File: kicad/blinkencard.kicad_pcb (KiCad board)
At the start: 2 copper layers, 88.9 x 50.8 mm, 94 parts, among them J1 USB_B_Micro, J2 Conn_02x04_Odd_Even, Q1 BC847, Q2 BC847, Q3 BC847, Q4 BC847, Q5 BC847, SW1 0, SW2 1, SW3 LEFT, SW4 RIGHT, U1 ICE40UP5K-SG48ITR, U2 ESP32-WROOM-32, U3 AP7361C-33E, U4 MIC5504-1.2YM5

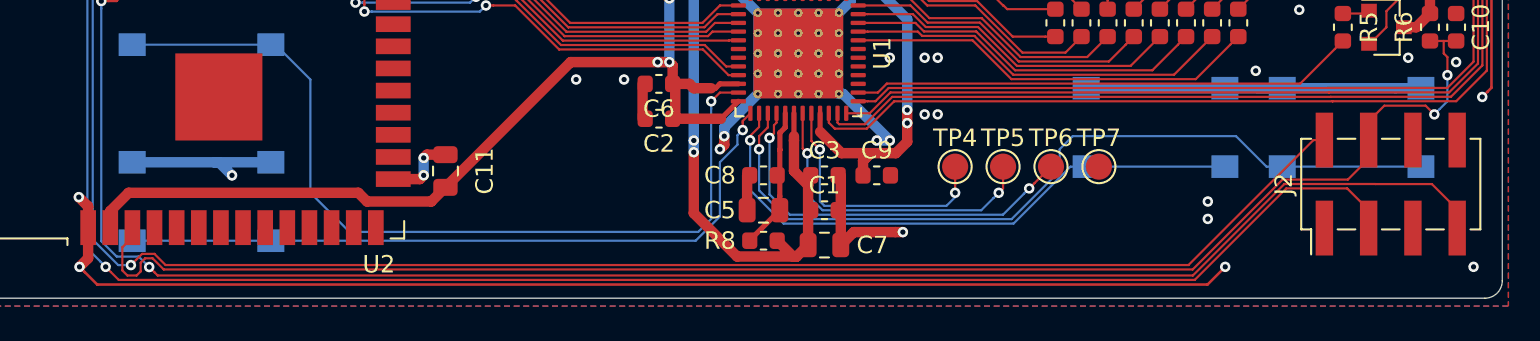
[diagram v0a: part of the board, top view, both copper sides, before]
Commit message: Fix RESET and GPIO0 (bootload) on the programming header to match an actual ESP-01 programmer
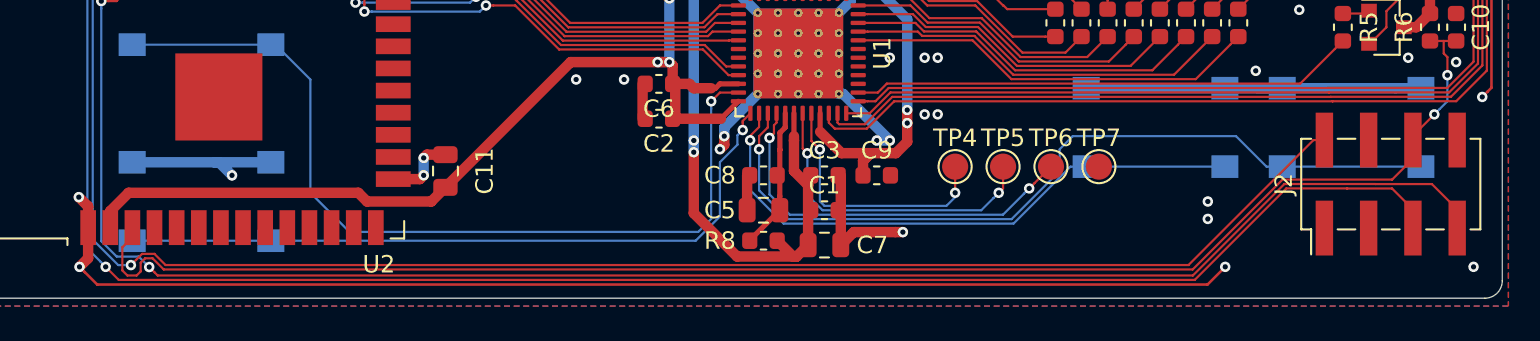
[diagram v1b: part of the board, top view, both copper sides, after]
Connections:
- J2 pad 3: ESP_BOOTLOADER -> Net-(J2-Pad3)
- J2 pad 4: ESP_EN -> Net-(J2-Pad4)
- J2 pad 5: Net-(J2-Pad5) -> ESP_BOOTLOADER
- J2 pad 6: Net-(J2-Pad6) -> ESP_EN
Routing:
- net ESP_BOOTLOADER: track 113.6 -> 116.1 mm
- net Net-(J2-Pad4): track 0.00 -> 2.15 mm
- net Net-(J2-Pad6): track 1.07 -> 0.00 mm
- net Net-(J2-Pad3): track 0.00 -> 1.05 mm
- net ESP_EN: track 90.5 -> 89.6 mm

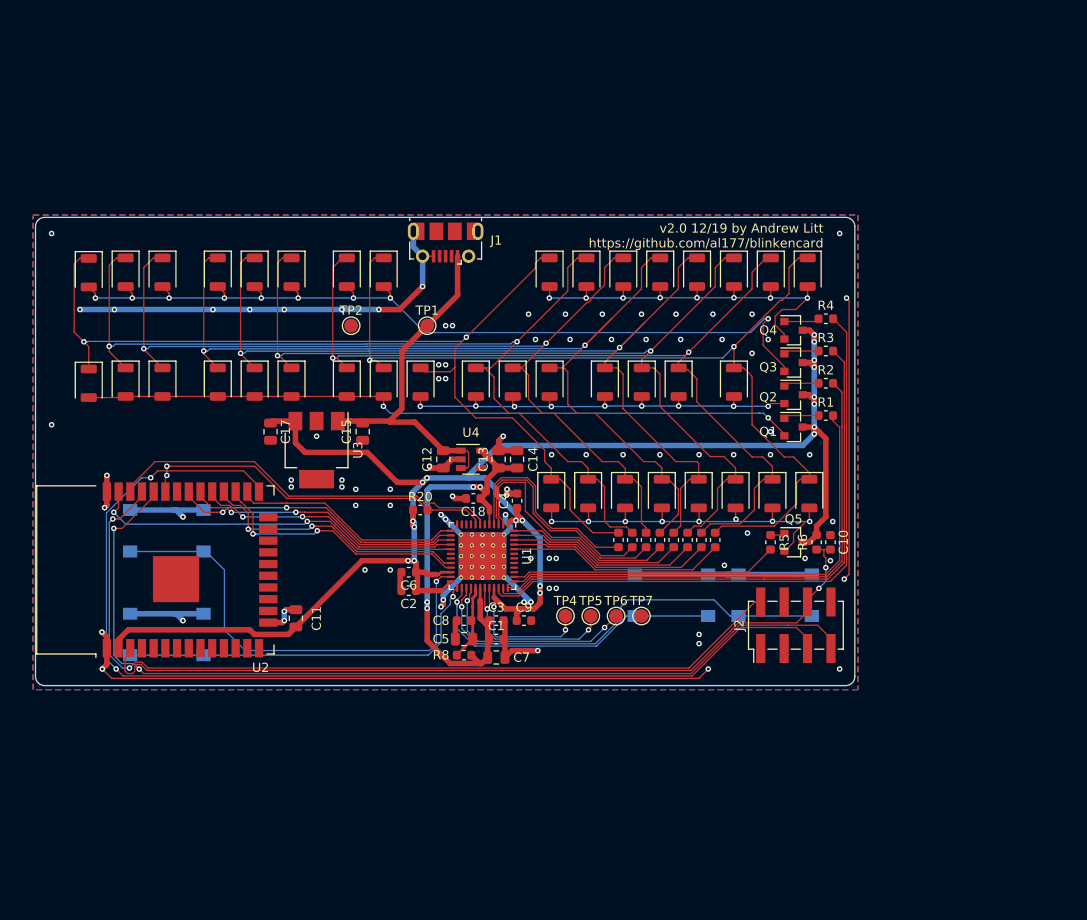
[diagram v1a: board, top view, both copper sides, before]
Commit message: Finish converting to ESP32, start on adding LiPo power
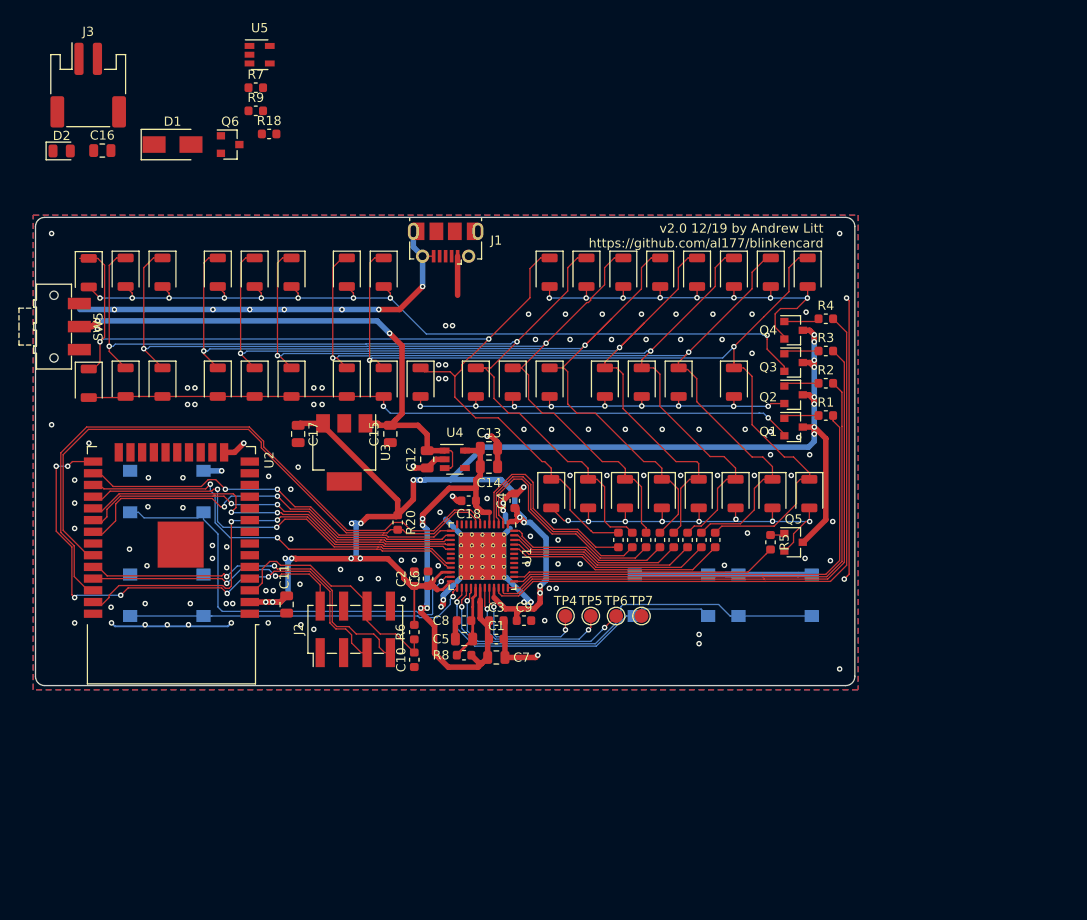
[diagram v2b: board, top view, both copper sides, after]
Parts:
- removed TP1: +5V, TestPoint:TestPoint_Pad_D1.5mm
- removed TP2: GND, TestPoint:TestPoint_Pad_D1.5mm
- added C16: 10.0uF, Capacitor_SMD:C_0805_2012Metric, F.Cu at (7.25, -7.25)
- added D1: B120-E3, Diode_SMD:D_SMA, F.Cu at (14.9, -7.90)
- added D2: LED_Small, LED_SMD:LED_0805_2012Metric, F.Cu at (2.84, -7.21)
- added J3: Conn_01x02, Connector_JST:JST_PH_S2B-PH-SM4-TB_1x02-1MP_P2.00mm_Horizontal, F.Cu at (5.72, -14.3)
- added Q6: DMG2301L, Package_TO_SOT_SMD:SOT-23, F.Cu at (21.1, -7.90)
- added R18: 1K, Resistor_SMD:R_0603_1608Metric, F.Cu at (25.4, -9.05)
- added R7: 100K, Resistor_SMD:R_0603_1608Metric, F.Cu at (23.9, -14.1)
- added R9: 10K, Resistor_SMD:R_0603_1608Metric, F.Cu at (23.9, -11.6)
- added SW5: SW_SPST, Button_Switch_SMD:SW_SPDT_CK-JS102011SAQN, F.Cu at (2.01, 11.8)
- added U5: MCP73831-2-OT, Package_TO_SOT_SMD:SOT-23-5, F.Cu at (24.3, -17.6)
- moved J2 47.8 mm to (34.7, 44.7)
- moved C10 46.9 mm to (41.1, 48.0), turned to 90 degrees
- moved R6 44.7 mm to (41.1, 45.0)
- moved SW1 4.25 mm to (14.2, 41.0)
- moved SW2 4.25 mm to (14.2, 29.8)
- moved U2 3.72 mm to (14.8, 34.8), turned to 180 degrees
- moved C14 3.15 mm to (49.2, 27.1), turned to 0 degrees
- moved C15 3.01 mm to (38.5, 23.5)
- moved C17 3.01 mm to (28.5, 23.5)
- moved U3 3.01 mm to (33.5, 25.5)
- moved R20 2.80 mm to (39.3, 33.1), turned to 270 degrees
- moved C6 2.21 mm to (42.6, 39.2), turned to 90 degrees
- moved C11 1.80 mm to (27.2, 42.0), turned to 270 degrees
- moved C12 1.75 mm to (42.5, 26.2)
- moved U4 1.75 mm to (45.5, 26.2)
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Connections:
- C12 pad 1: +5V -> VPP
- C15 pad 1: +5V -> VPP
- U3 pad 1: +5V -> VPP
- U4 pad 1: +5V -> VPP
- U4 pad 3: +5V -> VPP
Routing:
- net GND: track 242.5 -> 160.5 mm, vias 89 -> 133
- net ESP_TXD0: track 94.4 -> 28.6 mm
- net ESP_EN: track 89.6 -> 26.7 mm, vias 2 -> 0
- net ESP_RXD0: track 102.6 -> 39.8 mm
- net VPP: track 0.00 -> 60.7 mm, vias 0 -> 3
- net ESP_BOOTLOADER: track 116.1 -> 58.9 mm, vias 2 -> 6
- net +5V: track 39.1 -> 4.24 mm
- net FPGA_CDONE: track 42.8 -> 71.0 mm
- net FPGA_CRESET: track 39.2 -> 65.6 mm, vias 2 -> 0
- net FPGA_INT: track 25.0 -> 41.5 mm, vias 0 -> 2
- net FPGA_TXO: track 28.7 -> 44.0 mm
- net FPGA_RXI: track 29.4 -> 44.3 mm
- net FPGA_SS: track 28.8 -> 42.6 mm
- net FPGA_SO: track 31.8 -> 43.7 mm
- net FPGA_SCK: track 30.1 -> 41.6 mm
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
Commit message: First pass routing complete w/ LiPo charging
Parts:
- added TP1: +5V, TestPoint:TestPoint_Pad_D1.5mm, F.Cu at (42.0, 8.50)
- added TP2: GND, TestPoint:TestPoint_Pad_D1.5mm, F.Cu at (47.0, 8.50)
- moved J3 40.6 mm to (10.2, 26.0)
- moved D2 35.8 mm to (37.5, 1.75), turned to 180 degrees
- moved U5 34.0 mm to (6.75, 11.5), turned to 90 degrees
- moved R7 33.3 mm to (49.8, 7.00), turned to 270 degrees
- moved J2 29.7 mm to (5.00, 45.5), turned to 0 degrees
- moved R9 29.1 mm to (3.25, 9.00), turned to 270 degrees
- moved C12 24.2 mm to (66.5, 23.2), turned to 0 degrees
- moved SW5 22.9 mm to (2.25, 34.8)
- moved Q6 22.1 mm to (10.5, 11.5), turned to 270 degrees
- moved C16 20.8 mm to (3.75, 13.2), turned to 90 degrees
- moved D1 19.4 mm to (16.0, 11.5)
- moved U4 16.2 mm to (61.5, 24.0), turned to 90 degrees
- moved U3 14.8 mm to (48.2, 25.5), turned to 0 degrees
- moved C17 14.3 mm to (42.2, 27.5), turned to 90 degrees
- moved R18 13.8 mm to (34.0, 1.75), turned to 180 degrees
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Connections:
- net Net-(D1-Pad1) renamed /wifi_and_power/UNSWITCHED_VPP
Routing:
- net +5V: track 4.24 -> 61.9 mm, vias 0 -> 4
- net Net-(D2-Pad1): track 0.00 -> 49.9 mm
- net Net-(D10-Pad1): track 108.2 -> 144.6 mm
- net /wifi_and_power/UNSWITCHED_VPP: track 0.00 -> 35.5 mm, vias 0 -> 4
- net +BATT: track 0.00 -> 31.8 mm
- net VDD: track 185.6 -> 158.6 mm, vias 22 -> 19
- net Net-(D11-Pad1): track 105.5 -> 132.0 mm
- net ESP_BOOTLOADER: track 58.9 -> 37.6 mm, vias 6 -> 2
- net ESP_TXD0: track 28.6 -> 11.9 mm
- net VPP: track 60.7 -> 77.2 mm, vias 3 -> 4
- net ESP_EN: track 26.7 -> 42.4 mm, vias 0 -> 4
- net FPGA_SI: track 47.7 -> 32.2 mm
- net ESP_RXD0: track 39.8 -> 24.8 mm, vias 2 -> 4
- net GND: track 160.5 -> 173.4 mm, vias 133 -> 154
- net Net-(D12-Pad1): track 102.5 -> 115.2 mm
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
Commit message: Layout complete for v2 build. Needs review.
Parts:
- added REF**: OSHW-Symbol_6.7x6mm_Copper, Symbol:OSHW-Symbol_6.7x6mm_Copper, F.Cu at (83.2, 46.5)
- moved D2 4.44 mm to (33.1, 1.80), turned to 0 degrees
- moved R18 2.31 mm to (36.3, 2.00), turned to 0 degrees
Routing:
- net GND: track 173.4 -> 189.5 mm, vias 154 -> 155
- net Net-(D2-Pad1): track 49.9 -> 40.8 mm
- net Net-(D30-Pad2): track 94.1 -> 87.9 mm, vias 9 -> 10
- net +5V: track 61.9 -> 63.6 mm
- net ESP_EN: track 42.4 -> 43.6 mm
- net ESP_TXD0: track 11.9 -> 10.8 mm
- net FPGA_TXO: track 37.6 -> 37.1 mm
- net ESP_BOOTLOADER: track 37.6 -> 37.1 mm
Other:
- board text added: "CHARGE"

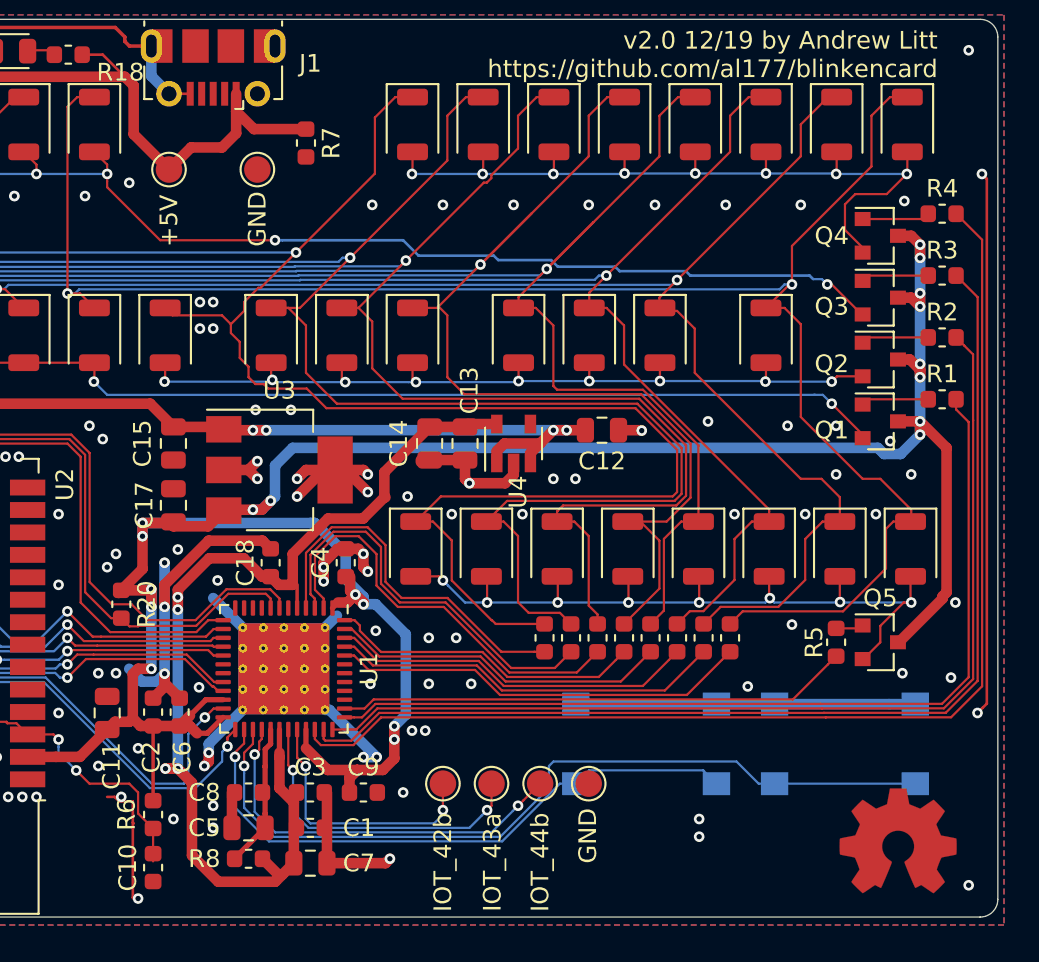
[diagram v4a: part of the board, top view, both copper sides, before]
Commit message: Add cap across 5V for charger
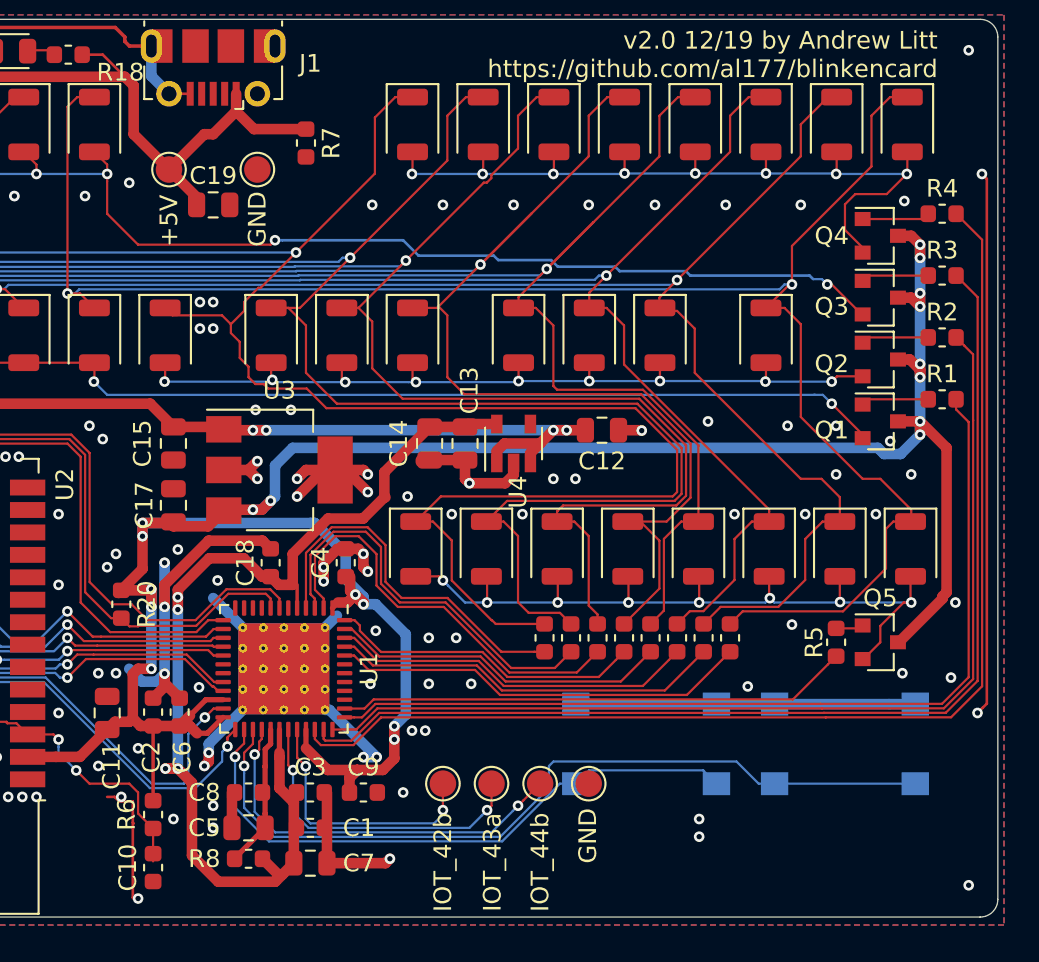
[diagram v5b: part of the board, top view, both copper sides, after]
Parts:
- removed REF**: OSHW-Symbol_6.7x6mm_Copper, Symbol:OSHW-Symbol_6.7x6mm_Copper
- added C19: 10.0uF, Capacitor_SMD:C_0805_2012Metric, F.Cu at (44.5, 10.5)
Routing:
- net +5V: track 63.6 -> 65.5 mm
- net Net-(D30-Pad2): track 87.9 -> 89.0 mm

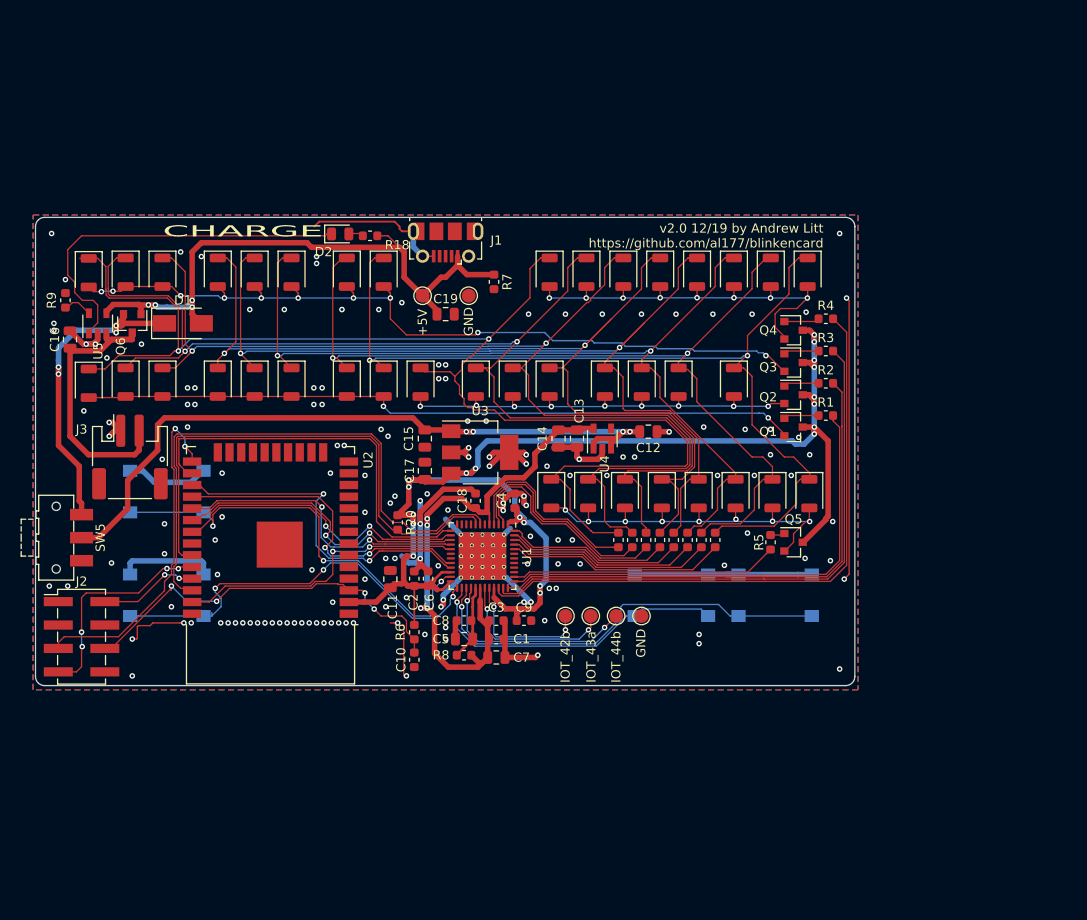
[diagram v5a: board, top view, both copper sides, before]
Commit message: v2.0 release - clean silk, add order number placeholder for JLCPCB, add MFG PN in components for BOM, add BOM, add STEP, generate fab outputs
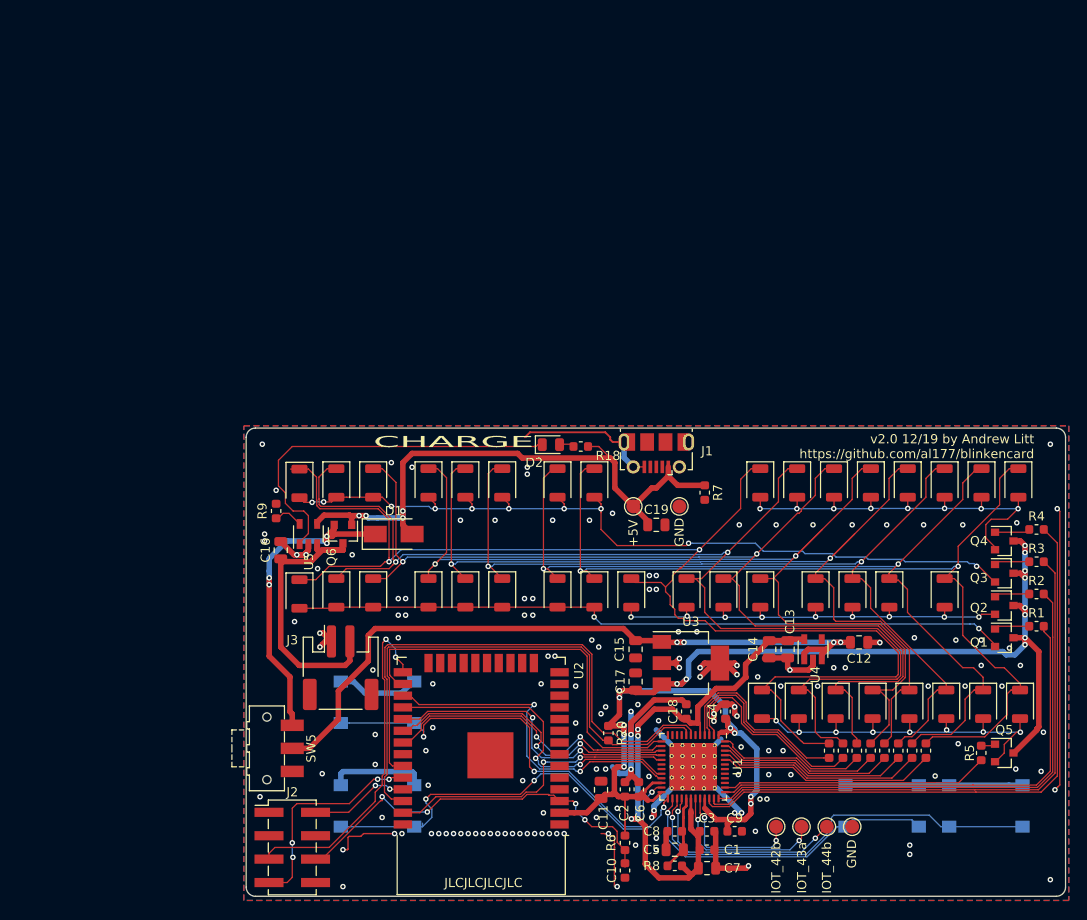
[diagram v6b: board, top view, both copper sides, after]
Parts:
- moved C1 32.3 mm to (72.9, 68.6)
- moved C10 32.3 mm to (64.0, 70.9)
- moved C11 32.3 mm to (61.4, 62.1)
- moved C12 32.3 mm to (89.4, 46.1)
- moved C13 32.3 mm to (81.6, 46.9)
- moved C14 32.3 mm to (79.6, 46.9)
- moved C15 32.3 mm to (65.1, 46.9)
- moved C16 32.3 mm to (26.6, 36.1)
- moved C17 32.3 mm to (65.1, 50.4)
- moved C18 32.3 mm to (70.6, 53.6)
- moved C19 32.3 mm to (67.4, 33.4)
- moved C2 32.3 mm to (64.0, 62.1)
- moved C3 32.3 mm to (72.9, 66.6)
- moved C4 32.3 mm to (74.9, 53.6)
- moved C5 32.3 mm to (69.4, 68.6)
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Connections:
- U2 pad 39: (no net) -> GND
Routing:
- net GND: vias 155 -> 154
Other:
- board text added: "JLCJLCJLCJLC"
